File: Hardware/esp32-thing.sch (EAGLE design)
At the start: 67 parts, among them Q1 2.5A/30V, Q2 MBT3904DW1T1, U1 MCP73831, U3 AP2112K-3.3V, U4 FT231XS, U5 W25Q32FVSS, Y1 26MHz, Y2 32.768kHz

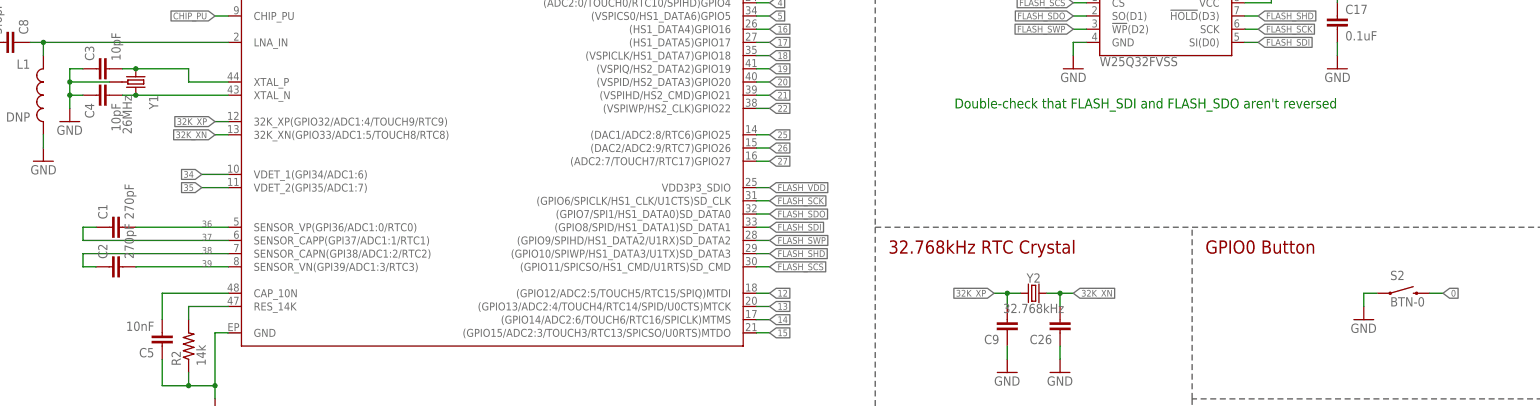
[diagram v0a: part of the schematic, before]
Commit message: Cleaning up schematic.
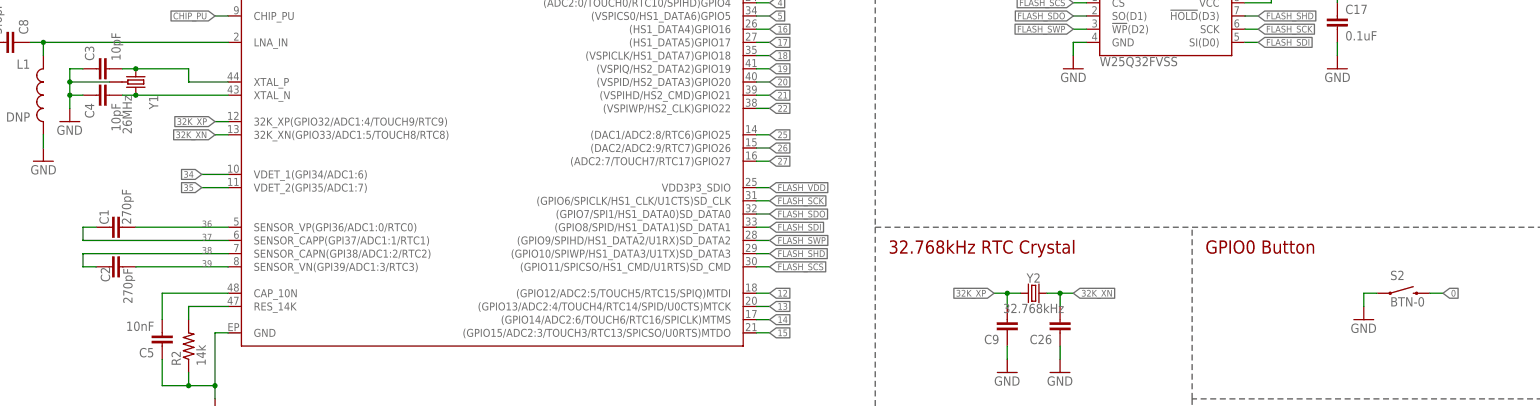
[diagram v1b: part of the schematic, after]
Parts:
- J1: device SparkFun-Connectors:M20NO_SILK_KIT -> SparkFun-Connectors:M20NOSILK
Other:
- note removed: "Double-check that FLASH_SDI and FLASH_SDO aren't reversed"
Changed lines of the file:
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@@
 <part name="GND20" library="SparkFun-Aesthetics" deviceset="GND" device=""/>
 <part name="GND23" library="SparkFun-Aesthetics" deviceset="GND" device=""/>
-<part name="J1" library="SparkFun-Connectors" deviceset="M20" device="NO_SILK_KIT"/>
+<part name="J1" library="SparkFun-Connectors" deviceset="M20" device="NOSILK"/>
 <part name="J2" library="SparkFun-Connectors" deviceset="M20" device="NOSILK"/>
 <part name="S2" library="SparkFun-Electromechanical" deviceset="SWITCH-MOMENTARY-2" device="SMD-4.6X2.8MM" value="BTN-0"/>
@@
 <sheet>
 <plain>
-<text x="213.36" y="121.92" size="1.905" layer="91">Double-check that FLASH_SDI and FLASH_SDO aren't reversed</text>
 <text x="355.6" y="154.94" size="1.905" layer="91" font="vector">Boot Mode Configuration
 Pin        Default     Boot   Download
@@
 <instance part="C3" gate="G$1" x="50.8" y="129.54" rot="R90"/>
 <instance part="C4" gate="G$1" x="50.8" y="124.46" rot="MR270"/>
-<instance part="C1" gate="G$1" x="53.34" y="99.06" rot="R90"/>
-<instance part="C2" gate="G$1" x="53.34" y="91.44" rot="R90"/>
+<instance part="C1" gate="G$1" x="53.34" y="99.06" smashed="yes" rot="R90">
+<attribute name="NAME" x="50.673" y="99.568" size="1.778" layer="95" rot="R90"/>
+<attribute name="VALUE" x="54.991" y="99.568" size="1.778" layer="96" rot="R90"/>
+</instance>
+<instance part="C2" gate="G$1" x="53.34" y="91.44" smashed="yes" rot="R90">
+<attribute name="NAME" x="49.149" y="91.44" size="1.778" layer="95" rot="R270"/>
+<attribute name="VALUE" x="53.467" y="91.186" size="1.778" layer="96" rot="R270"/>
+</instance>
 <instance part="C5" gate="G$1" x="60.96" y="78.74" rot="R180"/>
 <instance part="R2" gate="G$1" x="66.04" y="76.2" rot="R90"/>

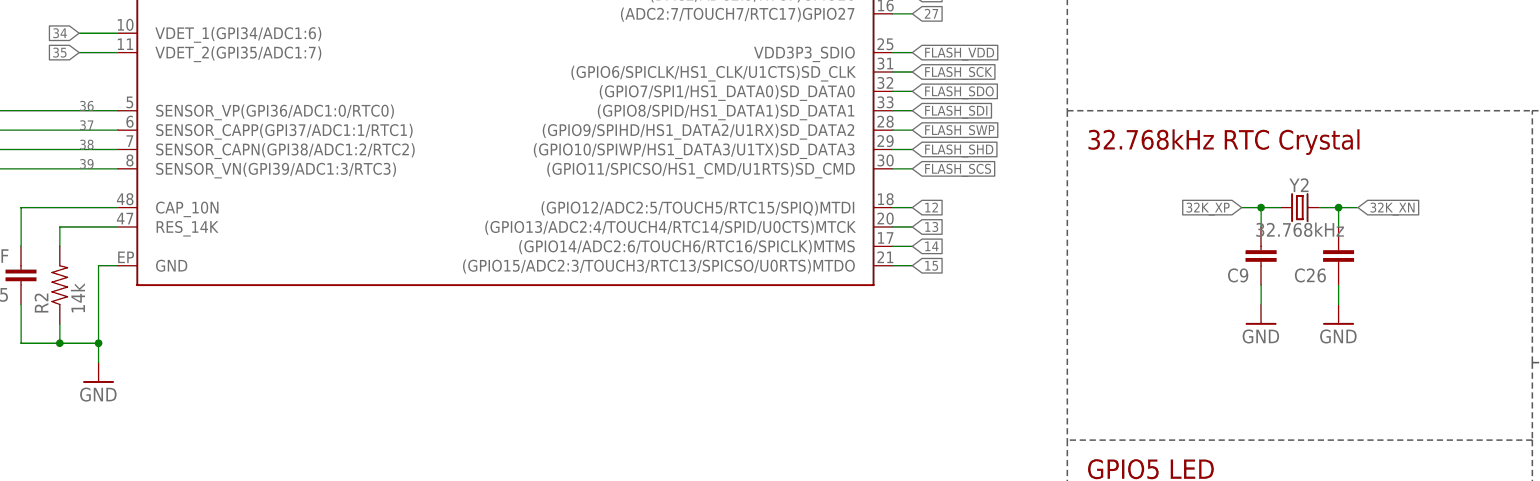
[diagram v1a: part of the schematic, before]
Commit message: Adding PROD_IDs to new parts, adding new parts to temp library.
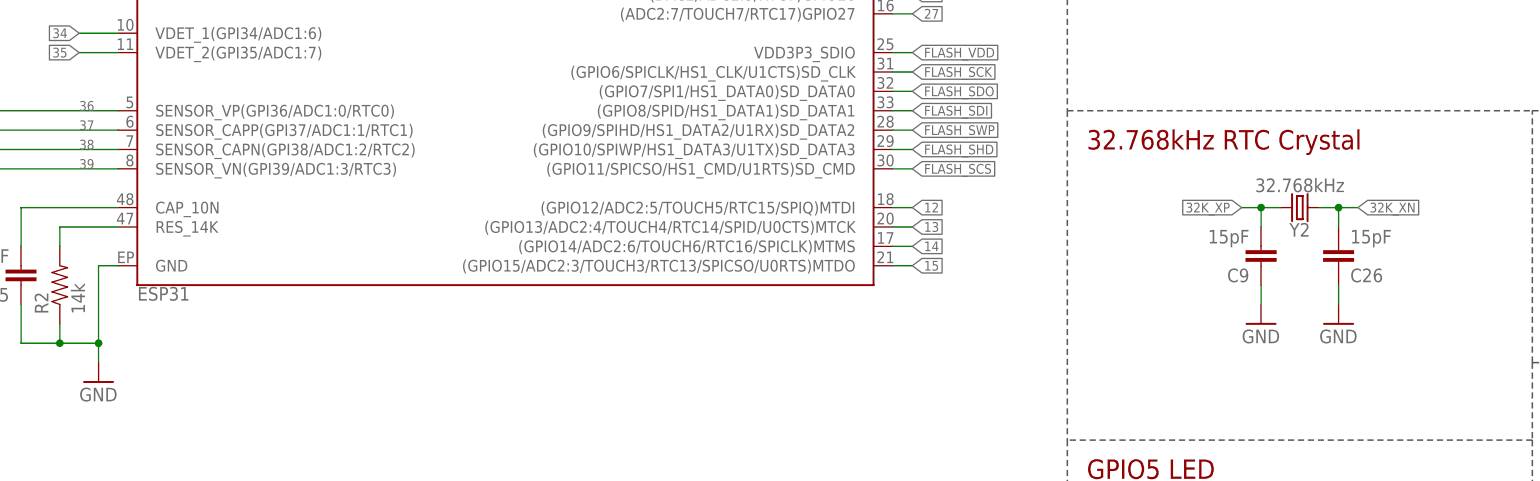
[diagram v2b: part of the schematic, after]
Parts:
- C1, C2: device SparkFun-Capacitors:CAP0603-CAP -> esp32-thing-temp:270PF-50V-5%(0603)
- C26, C9: value (none) -> 15pF; device SparkFun-Passives:CAP0603-CAP -> SparkFun-Capacitors:15PF-0603-50V-5%
- R2: device SparkFun-Passives:RESISTOR0603-RES -> esp32-thing-temp:14KOHM-1/10W-1%(0603)
- U2: value (none) -> ESP31
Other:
- moved on the sheet: Y2

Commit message: Misc changes after running through checklist.
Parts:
- added FD1, FD2: FIDUCIAL1X2, SparkFun-Aesthetics:FIDUCIAL1X2
- added LOGO3: SFE_LOGO_NAME.1_INCH, SparkFun-Aesthetics:SFE_LOGO_NAME.1_INCH
- C1, C2: value 270pF -> 270PF-50V-5%(0603)
- C10: device SparkFun-Capacitors:2.2UF-10V-20%(0603) -> SparkFun-Capacitors:2.2UF-0603-10V-20%
- C11, C14, C16, C17, C18, C20, C21, C23, C25: device SparkFun-Capacitors:0.1UF-25V(+80/-20%)(0603) -> SparkFun-Capacitors:0.1UF-0603-25V-(+80/-20%)
- C12, C13: device SparkFun-Capacitors:47PF-50V-5%(0603) -> SparkFun-Capacitors:47PF-0603-50V-5%
- C19, C6: device SparkFun-Capacitors:4.7UF-6.3V-10%(0603)0603 -> SparkFun-Capacitors:4.7UF0603
- C22: device SparkFun-Capacitors:10UF-6.3V-20%(0603) -> SparkFun-Capacitors:10UF-0603-6.3V-20%
- C24: device SparkFun-Capacitors:1.0UF-16V-10%(0603) -> SparkFun-Capacitors:1.0UF-0603-16V-10%
- C3, C4: device SparkFun-Capacitors:10PF-50V-5%(0603) -> SparkFun-Capacitors:10PF-0603-50V-5%
- C5: device SparkFun-Capacitors:10NF/10000PF-50V-10%(0603) -> SparkFun-Capacitors:10NF-0603-50V-10%
- C7: device SparkFun-Capacitors:1.0UF-25V-+80/-20(0805)" -> SparkFun-Capacitors:1.0UF-0805-25V-(+80/-20%)
- C8: device SparkFun-Capacitors:CAP0603-CAP -> esp32-thing-temp:5.6PF-50V-5%(0603)
- R17, R18, R7: value 10K -> 10k; device SparkFun-Resistors:10KOHM1/10W1%(0603)0603 -> SparkFun-Resistors:10KOHM-0603-1/10W-1%
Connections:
- net VUSB renamed VUSB-RAW
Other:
- note added: "ESP32 VCC Range: 2.8-3.6V"
- note added: "SJ2 disconnects the power LED (for power saving)."
- note added: "SJ3 allows selection between FLASH_VDD and 3.3V as the voltage supply to the flash IC."
- moved on the sheet: C10, C7, D2, D3, Q1, R4, R7, SJ2, U3

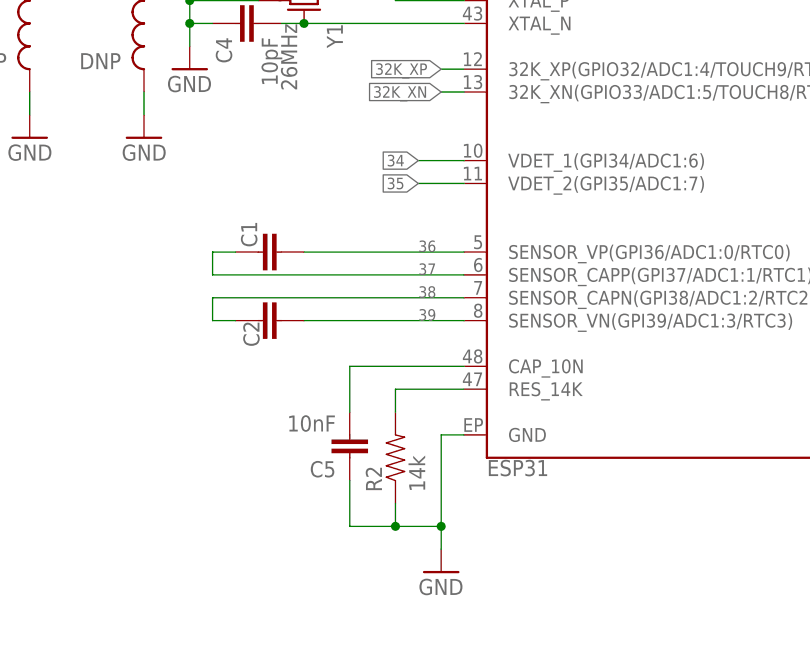
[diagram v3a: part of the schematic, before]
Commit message: Adding name, value to C1, C2. Updating IC value.
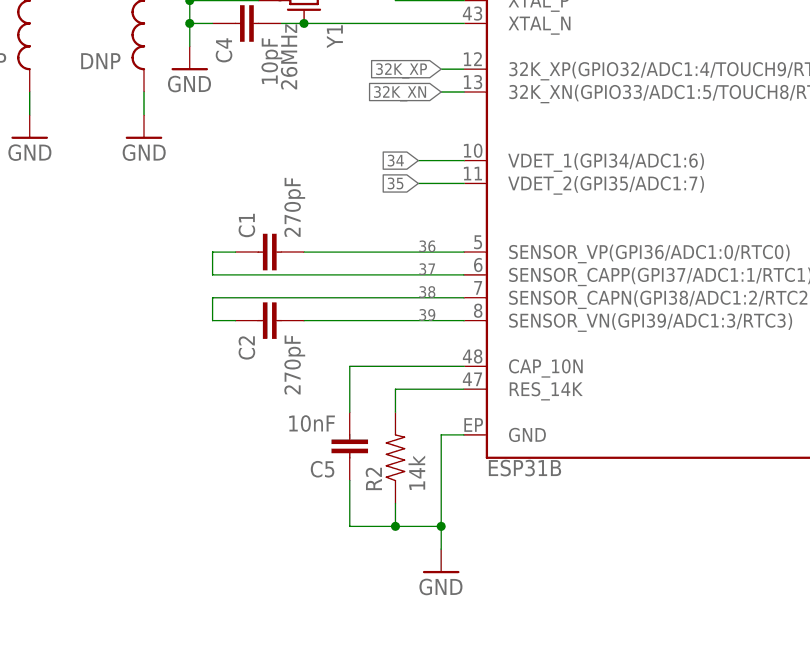
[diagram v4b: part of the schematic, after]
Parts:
- C1, C2: value 270PF-50V-5%(0603) -> 270pF
- U2: value ESP31 -> ESP31B
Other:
- moved on the sheet: C2

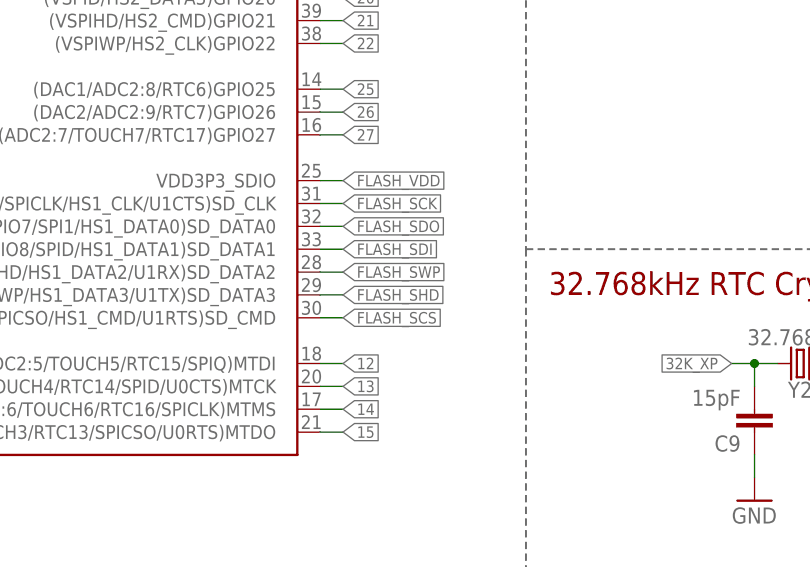
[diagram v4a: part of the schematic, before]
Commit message: Fixing NPN pin assignments, flash HD and SWP pin routes.
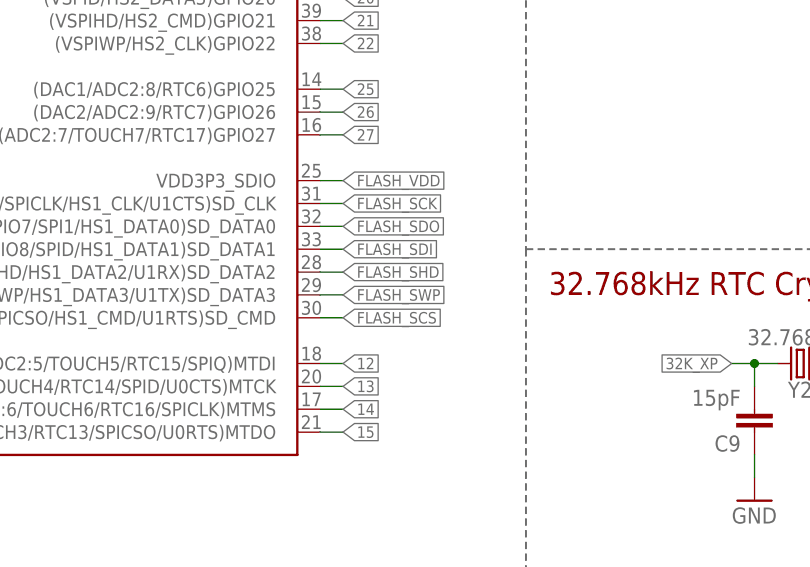
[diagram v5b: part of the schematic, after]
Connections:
- net FLASH_SHD: now also U2.(GPIO9/SPIHD/HS1_DATA2/U1RX)SD_DATA2; no longer U2.(GPIO10/SPIWP/HS1_DATA3/U1TX)SD_DATA3
- net FLASH_SWP: now also U2.(GPIO10/SPIWP/HS1_DATA3/U1TX)SD_DATA3; no longer U2.(GPIO9/SPIHD/HS1_DATA2/U1RX)SD_DATA2
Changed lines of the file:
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@@
 </segment>
 <segment>
-<wire x1="175.26" y1="96.52" x2="177.8" y2="96.52" width="0.1524" layer="91"/>
-<label x="177.8" y="96.52" size="1.27" layer="95" xref="yes"/>
-<pinref part="U2" gate="G$1" pin="(GPIO9/SPIHD/HS1_DATA2/U1RX)SD_DATA2"/>
+<wire x1="175.26" y1="93.98" x2="177.8" y2="93.98" width="0.1524" layer="91"/>
+<label x="177.8" y="93.98" size="1.27" layer="95" xref="yes"/>
+<pinref part="U2" gate="G$1" pin="(GPIO10/SPIWP/HS1_DATA3/U1TX)SD_DATA3"/>
 </segment>
 </net>
@@
 </segment>
 <segment>
-<wire x1="175.26" y1="93.98" x2="177.8" y2="93.98" width="0.1524" layer="91"/>
-<label x="177.8" y="93.98" size="1.27" layer="95" xref="yes"/>
-<pinref part="U2" gate="G$1" pin="(GPIO10/SPIWP/HS1_DATA3/U1TX)SD_DATA3"/>
+<wire x1="175.26" y1="96.52" x2="177.8" y2="96.52" width="0.1524" layer="91"/>
+<label x="177.8" y="96.52" size="1.27" layer="95" xref="yes"/>
+<pinref part="U2" gate="G$1" pin="(GPIO9/SPIHD/HS1_DATA2/U1RX)SD_DATA2"/>
 </segment>
 </net>

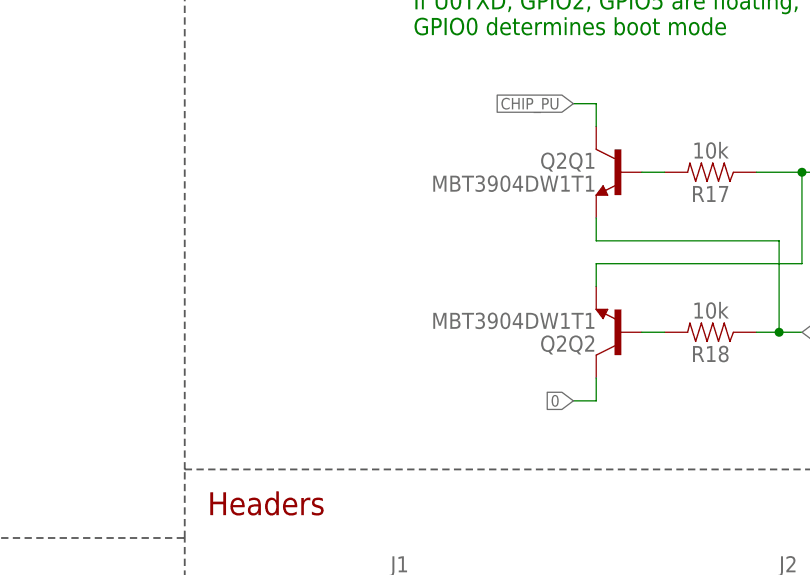
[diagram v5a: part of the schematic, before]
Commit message: Added GPIO0 pullup
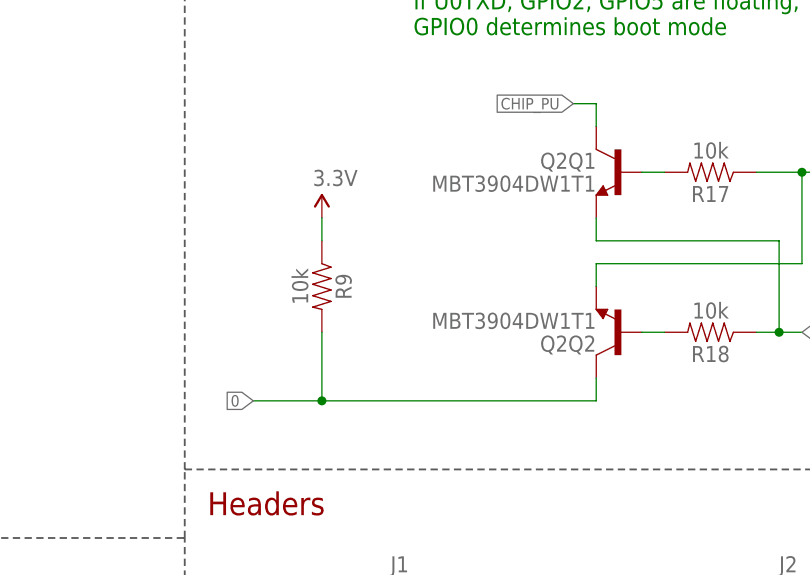
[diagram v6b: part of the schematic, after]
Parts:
- added R9: 10k, SparkFun-Resistors:10KOHM-0603-1/10W-1%
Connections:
- net 0: now also R9.2
- net 3.3V: now also R9.1
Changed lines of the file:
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@@
 <?xml version="1.0" encoding="utf-8"?>
 <!DOCTYPE eagle SYSTEM "eagle.dtd">
-<eagle version="7.5.0">
+<eagle version="7.6.0">
 <drawing>
 <settings>
@@
 <layer number="255" name="routoute" color="7" fill="1" visible="yes" active="yes"/>
 </layers>
-<schematic xreflabel="%F%N/%S" xrefpart="/%S.%C%R">
+<schematic xreflabel="%F%N/%S" xrefpart="1_/%S.%C%R">
 <attributes>
 </attributes>
@@
 <part name="SUPPLY15" library="SparkFun-Aesthetics" deviceset="V_BATT" device=""/>
 <part name="LOGO3" library="SparkFun-Aesthetics" deviceset="SFE_LOGO_NAME" device=".1_INCH" value="SFE_LOGO_NAME.1_INCH"/>
+<part name="R9" library="SparkFun-Resistors" deviceset="10KOHM" device="-0603-1/10W-1%" value="10k"/>
+<part name="SUPPLY17" library="SparkFun-Aesthetics" deviceset="3.3V" device=""/>
 </parts>
 <sheets>
@@
 </instance>
 <instance part="LOGO3" gate="G$1" x="271.78" y="2.54"/>
+<instance part="R9" gate="G$1" x="345.44" y="127" rot="R270"/>
+<instance part="SUPPLY17" gate="G$1" x="345.44" y="134.62"/>
 </instances>
 <busses>
@@
 <wire x1="416.56" y1="53.34" x2="416.56" y2="55.88" width="0.1524" layer="91"/>
 </segment>
+<segment>
+<pinref part="SUPPLY17" gate="G$1" pin="3.3V"/>
+<pinref part="R9" gate="G$1" pin="1"/>
+<wire x1="345.44" y1="134.62" x2="345.44" y2="132.08" width="0.1524" layer="91"/>
+</segment>
 </net>
 <net name="CHIP_PU" class="0">
@@
 </segment>
 <segment>
-<wire x1="375.92" y1="114.3" x2="373.38" y2="114.3" width="0.1524" layer="91"/>
-<label x="373.38" y="114.3" size="1.27" layer="95" rot="R180" xref="yes"/>
+<wire x1="375.92" y1="114.3" x2="345.44" y2="114.3" width="0.1524" layer="91"/>
+<label x="337.82" y="114.3" size="1.27" layer="95" rot="R180" xref="yes"/>
 <pinref part="Q2" gate="Q2" pin="C"/>
+<wire x1="345.44" y1="114.3" x2="337.82" y2="114.3" width="0.1524" layer="91"/>
 <wire x1="375.92" y1="114.3" x2="375.92" y2="116.84" width="0.1524" layer="91"/>
-</segment>
-<segment>
+<pinref part="R9" gate="G$1" pin="2"/>
+<wire x1="345.44" y1="121.92" x2="345.44" y2="114.3" width="0.1524" layer="91"/>
+<junction x="345.44" y="114.3"/>
+</segment>
+<segment>
